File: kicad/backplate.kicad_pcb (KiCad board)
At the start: 2 copper layers, 28 x 100 mm, 7 parts, among them J1 10018784-10210TLF

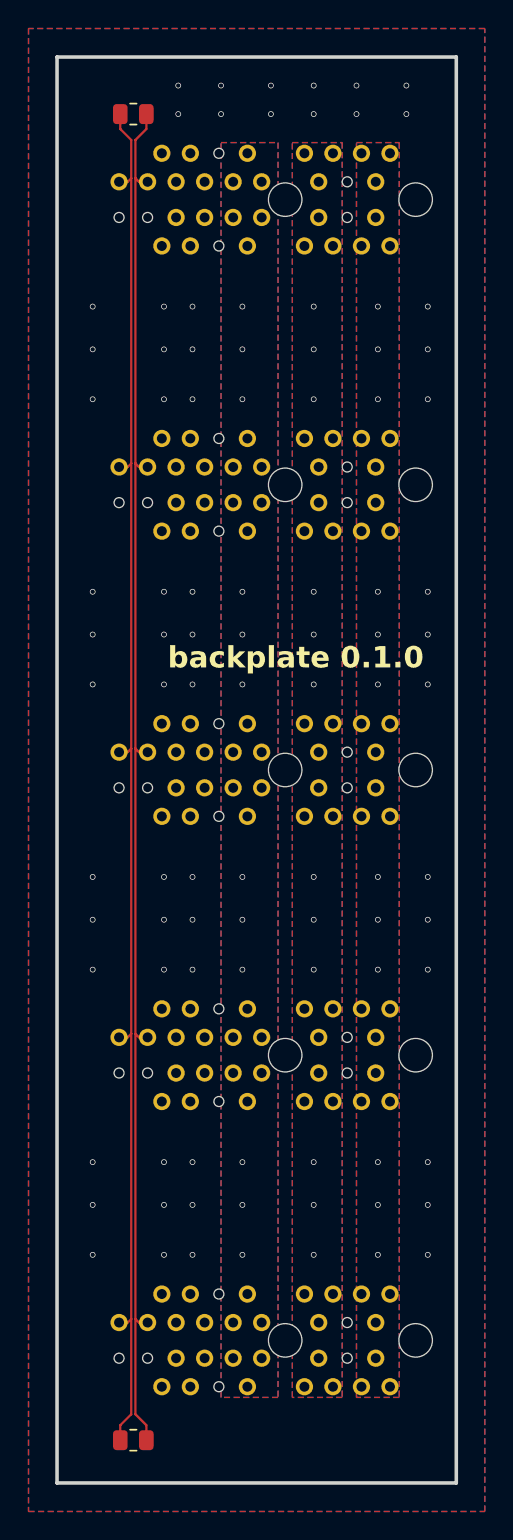
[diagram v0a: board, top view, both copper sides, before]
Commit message: modified backplate to 2 PCIe
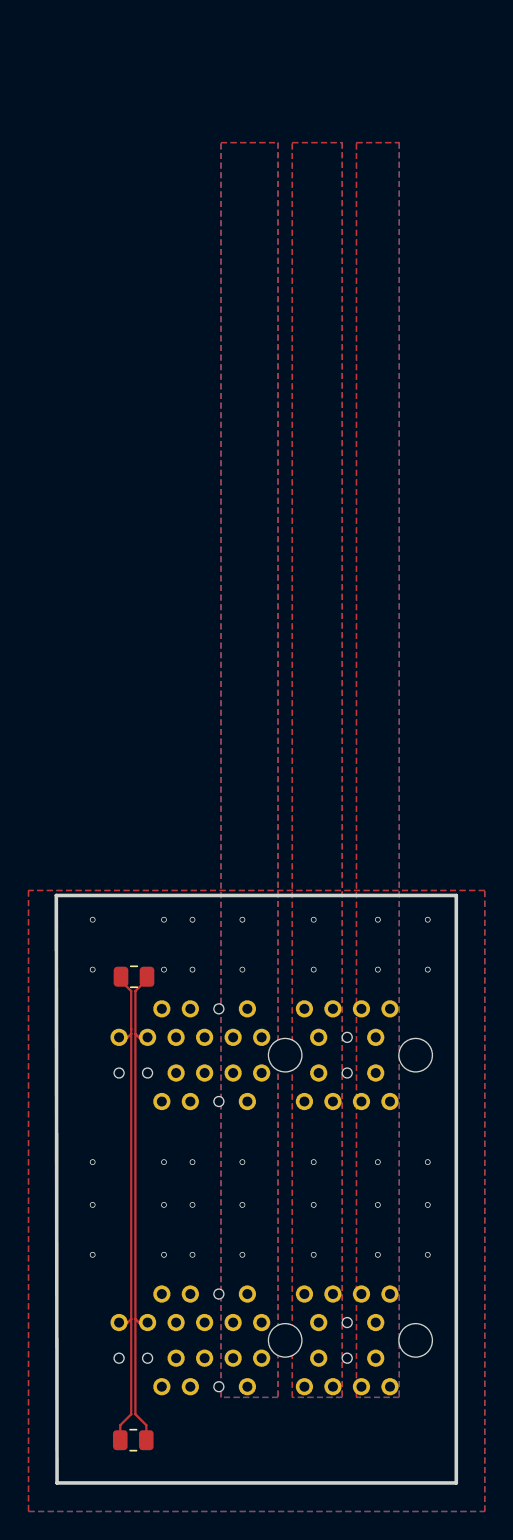
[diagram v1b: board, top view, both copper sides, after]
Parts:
- removed the J1 at (138.0, 60.0)
- removed the J1 at (138.0, 80.0)
- removed the J1 at (138.0, 100.0)
- moved R1 60.5 mm to (127.4, 114.5)
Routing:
- net CANP: track 98.4 -> 35.0 mm
- net CANN: track 98.4 -> 35.1 mm
- net GND: vias 60 -> 20
- net +7.4V: vias 12 -> 5
- net +5V: vias 12 -> 5
- net +3.3V: vias 12 -> 5
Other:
- board size 28 x 100 mm -> 28 x 41.2 mm
- board text removed: "backplate 0.1.0"
